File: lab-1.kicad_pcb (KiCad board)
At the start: 2 copper layers, 58.4 x 43.2 mm, 11 parts, among them U1 STM32F405RGTx

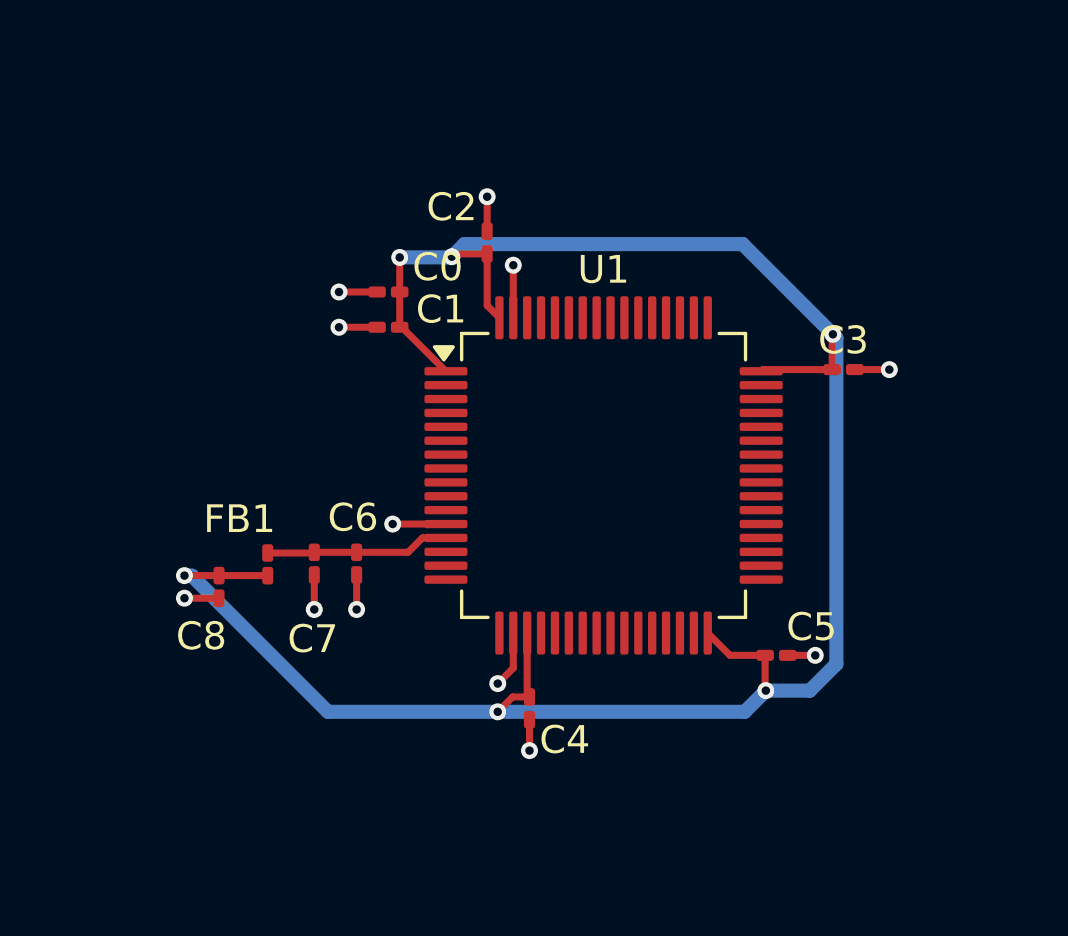
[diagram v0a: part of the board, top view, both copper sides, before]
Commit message: Changed the footprints + track width
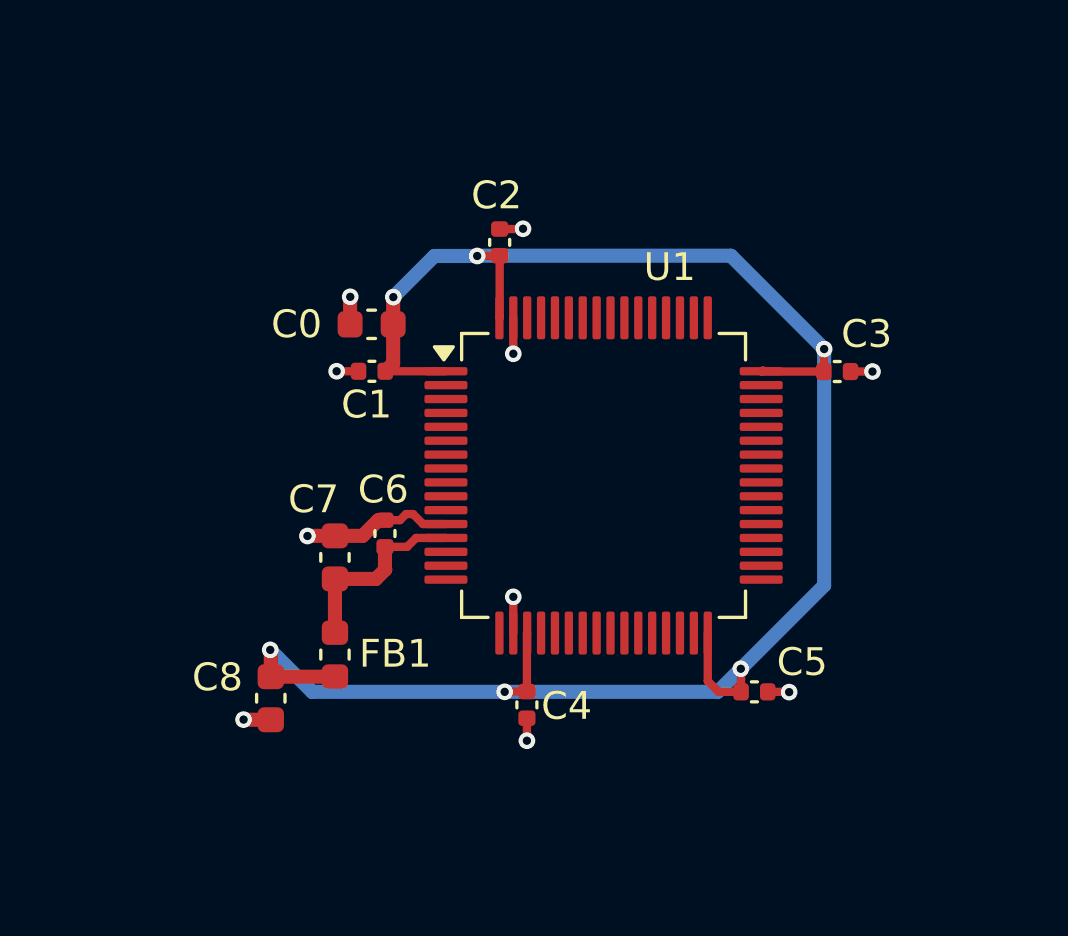
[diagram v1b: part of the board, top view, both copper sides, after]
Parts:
- C0, C7, C8: footprint Capacitor_SMD:C_0201_0603Metric_Pad0.64x0.40mm_HandSolder -> Capacitor_SMD:C_0603_1608Metric
- C1, C2, C3, C4, C5, C6: footprint Capacitor_SMD:C_0201_0603Metric_Pad0.64x0.40mm_HandSolder -> Capacitor_SMD:C_0402_1005Metric
- FB1: footprint Inductor_SMD:L_0201_0603Metric_Pad0.64x0.40mm_HandSolder -> Inductor_SMD:L_0603_1608Metric
- moved C8 4.42 mm to (145.5, 112.2)
- moved FB1 4.05 mm to (147.8, 110.6)
- moved C1 1.69 mm to (149.1, 100.4)
- moved C5 1.53 mm to (162.9, 111.9)
- moved C6 1.49 mm to (149.6, 106.2), turned to 90 degrees
- moved C0 1.31 mm to (149.1, 98.7)
- moved C7 0.78 mm to (147.8, 107.1), turned to 90 degrees
- moved C2 0.45 mm to (153.7, 95.8)
- moved C3 0.24 mm to (165.9, 100.4)
- moved C4 0.15 mm to (154.7, 112.4)
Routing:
- net +3.3V: track 78.2 -> 69.5 mm
- net GND: track 17.0 -> 14.0 mm, vias 12 -> 10

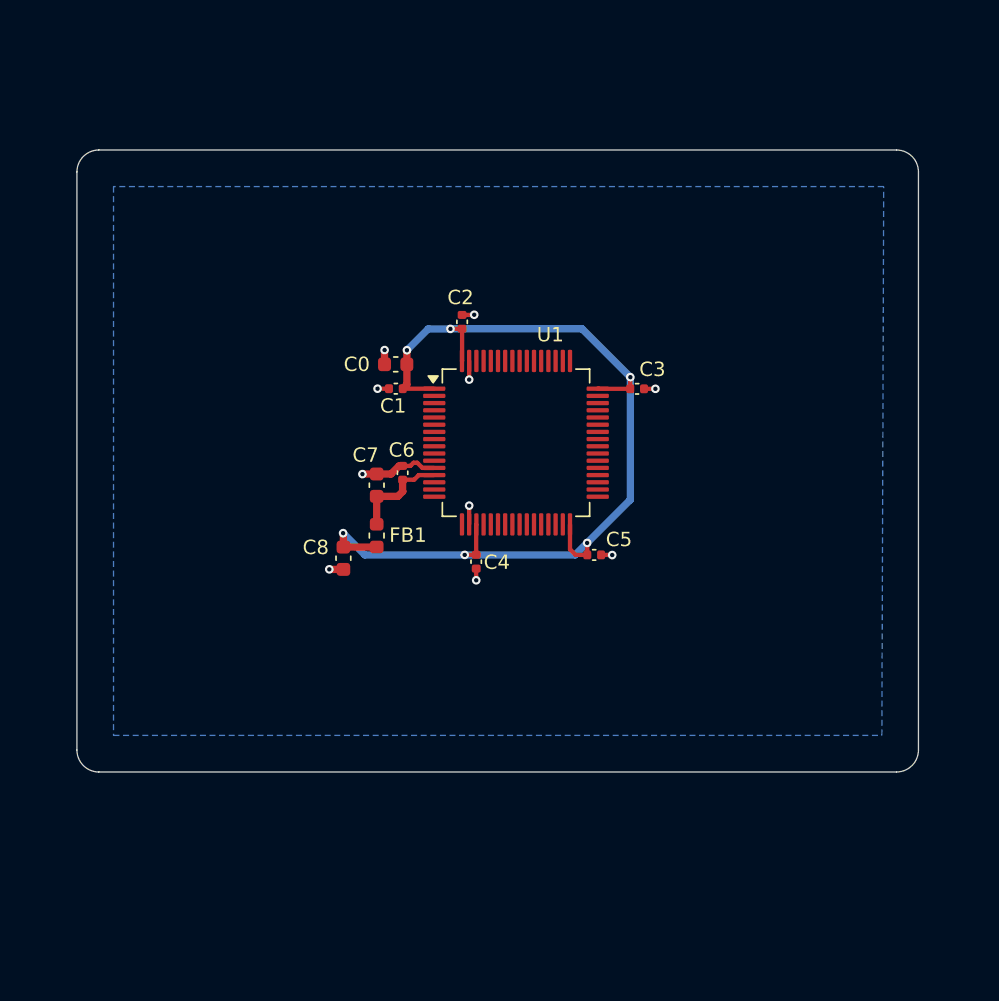
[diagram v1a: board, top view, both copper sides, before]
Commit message: Modified tracks and capacitor placing Added type-c and LDO MCP1700 as source of power for STM
Signed-off-by: Yehor Bilous <bilous801@gmail.com>
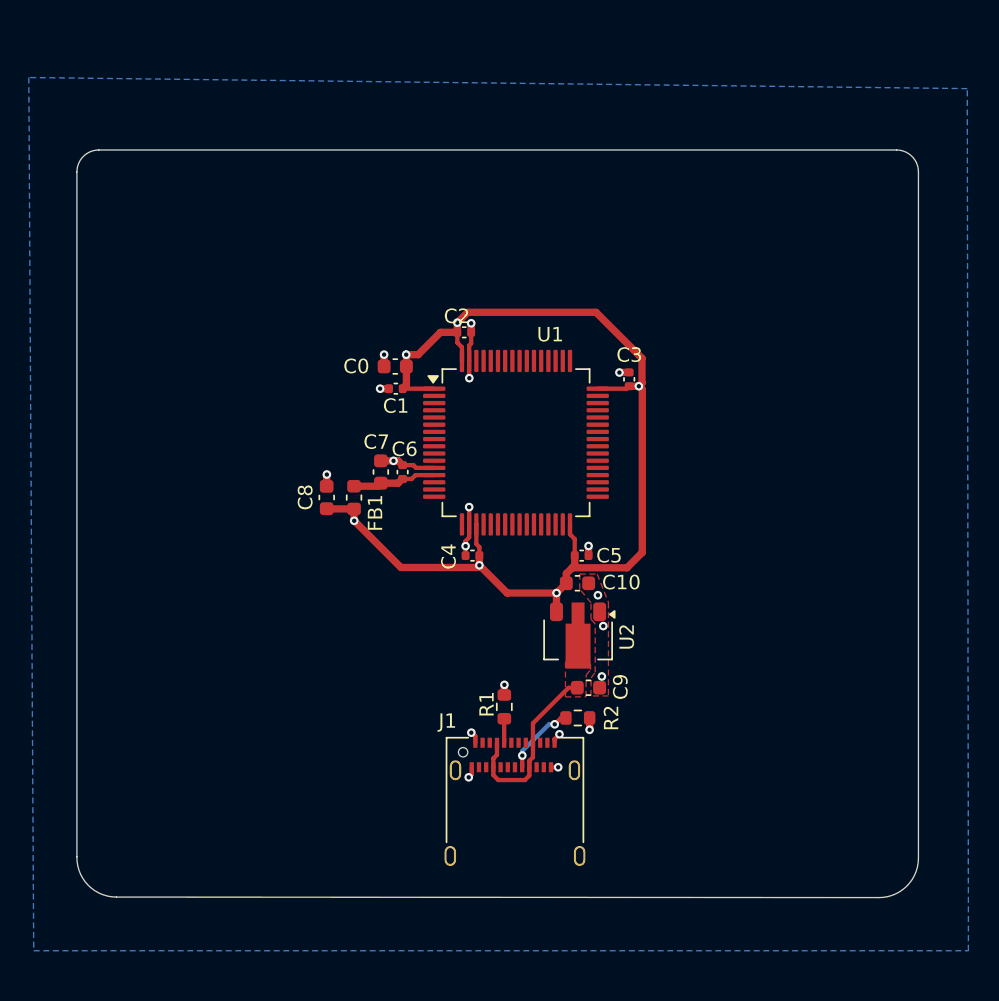
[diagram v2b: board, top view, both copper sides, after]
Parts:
- added C10: 1u, Capacitor_SMD:C_0603_1608Metric, F.Cu at (161.8, 113.9)
- added C9: 1u, Capacitor_SMD:C_0603_1608Metric, F.Cu at (162.5, 121.2)
- added J1: USB_C_Receptacle, Connector_USB:USB_C_Receptacle_Amphenol_12401610E4-2A, F.Cu at (157.4, 130.0)
- added R1: 5k1, Resistor_SMD:R_0603_1608Metric, F.Cu at (156.7, 122.5)
- added R2: 5k1, Resistor_SMD:R_0603_1608Metric, F.Cu at (161.8, 123.2)
- added U2: MCP1700x-120xxMB, Package_TO_SOT_SMD:SOT-89-3, F.Cu at (161.8, 117.8)
- C6: value 10n -> 100n
- FB1: value 120 -> ?
- moved C8 4.37 mm to (144.3, 107.9), turned to 90 degrees
- moved FB1 3.07 mm to (146.2, 108.0)
- moved C7 0.96 mm to (148.1, 106.2)
- moved C5 0.87 mm to (162.0, 112.0)
- moved C3 0.86 mm to (165.3, 99.7), turned to 90 degrees
- moved C2 0.75 mm to (153.9, 96.5), turned to 0 degrees
- moved C4 0.49 mm to (154.5, 112.0), turned to 180 degrees
- moved C0 0.15 mm to (149.1, 98.8)
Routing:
- net +5V: track 0.00 -> 13.0 mm
- net +3.3V: track 69.5 -> 76.7 mm
- net GND: track 14.0 -> 19.4 mm, vias 10 -> 19
- net Net-(J1-CC2): track 0.00 -> 5.10 mm, vias 0 -> 2
- net Net-(J1-CC1): track 0.00 -> 1.67 mm
- net +3.3VA: track 7.04 -> 5.88 mm
- added copper zone on F.Cu, net +5V
- added copper zone on F.Cu, net GND
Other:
- board size 58.4 x 43.2 mm -> 58.4 x 51.9 mm

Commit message: add a programmer header and power ORing
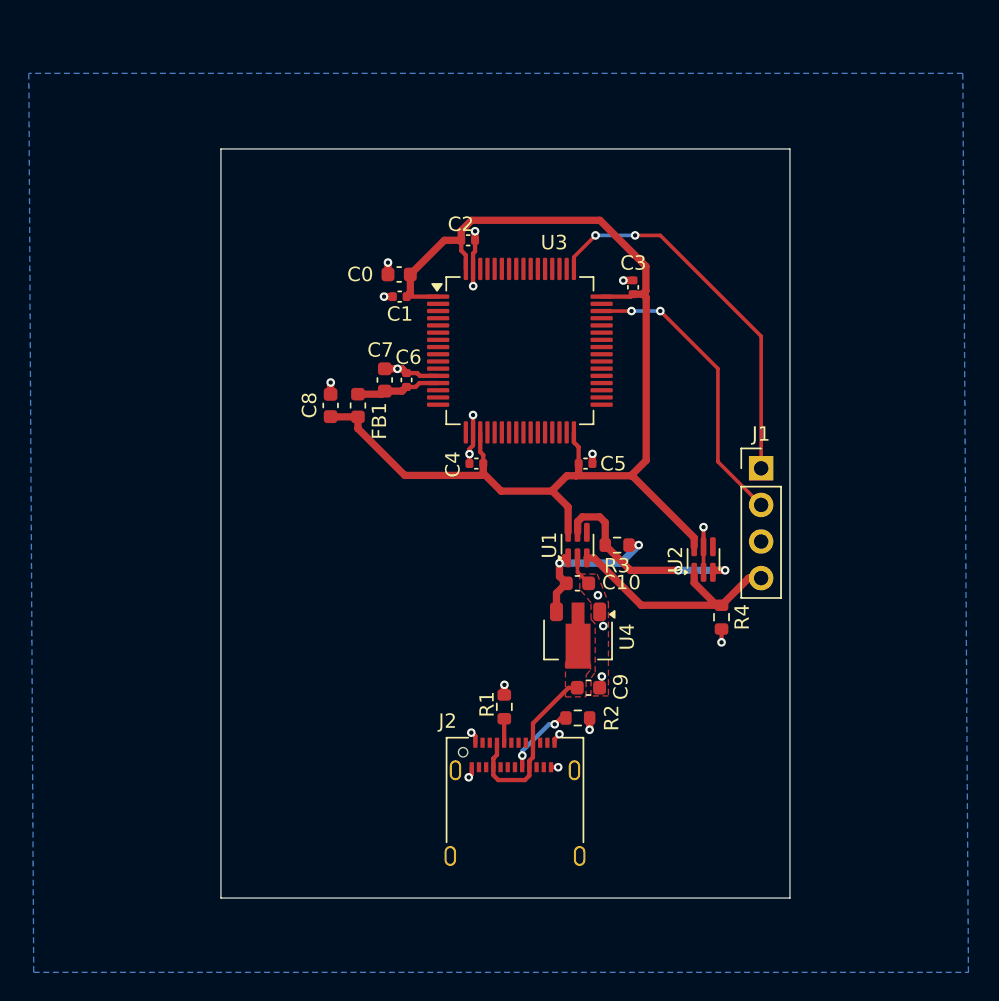
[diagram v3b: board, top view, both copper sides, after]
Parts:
- added J1: Conn_01x04_Pin, Connector_PinHeader_2.54mm:PinHeader_1x04_P2.54mm_Vertical, F.Cu at (174.5, 105.9)
- added R3: 10k, Resistor_SMD:R_0603_1608Metric, F.Cu at (164.5, 111.2)
- added R4: 100k, Resistor_SMD:R_0603_1608Metric, F.Cu at (171.8, 116.2)
- added U1: LM66100DCK, Package_TO_SOT_SMD:SOT-363_SC-70-6, F.Cu at (161.8, 111.2)
- added U2: LM66100DCK, Package_TO_SOT_SMD:SOT-363_SC-70-6, F.Cu at (170.5, 112.2)
- moved C0 6.40 mm to (149.4, 92.5)
- moved C1 6.40 mm to (149.4, 94.0)
- moved C2 6.40 mm to (154.2, 90.1)
- moved C3 6.40 mm to (165.6, 93.3)
- moved C4 6.40 mm to (154.7, 105.6)
- moved C5 6.40 mm to (162.3, 105.6)
- moved C6 6.40 mm to (149.9, 99.8)
- moved C7 6.40 mm to (148.4, 99.8)
- moved FB1 6.40 mm to (146.5, 101.6)
- moved U3 6.40 mm to (157.8, 97.8)
- moved C8 6.40 mm to (144.6, 101.6)
- renumbered J1 to J2, U1 to U3, U2 to U4
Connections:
- C10 pad 1: +3.3V -> +3.3V_LDO
- U3 pad 46: unconnected-(U1-PA13-Pad46) -> /SWDIO
- U3 pad 49: unconnected-(U1-PA14-Pad49) -> /SWCLK
- U4 pad 3: +3.3V -> +3.3V_LDO
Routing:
- net /SWCLK: track 0.00 -> 26.5 mm, vias 0 -> 2
- net /SWDIO: track 0.00 -> 20.4 mm, vias 0 -> 2
- net +3.3V_STLINK: track 0.00 -> 17.5 mm
- net Net-(U1-ST): track 0.00 -> 14.5 mm, vias 0 -> 2
- net +3.3V_LDO: track 0.00 -> 11.2 mm, vias 0 -> 2
- net +3.3V: track 76.7 -> 84.0 mm, vias 6 -> 0
- net GND: track 19.4 -> 25.6 mm, vias 19 -> 21
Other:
- board size 58.4 x 51.9 mm -> 39.5 x 52 mm

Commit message: add crystal
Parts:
- added C11: 22pF, Capacitor_SMD:C_0402_1005Metric, F.Cu at (146.0, 95.0)
- added C12: 22pF, Capacitor_SMD:C_0402_1005Metric, F.Cu at (146.0, 97.5)
- added Y1: 8 MHz, Crystal:Crystal_SMD_2520-4Pin_2.5x2.0mm, F.Cu at (148.9, 96.4)
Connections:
- U3 pad 5: unconnected-(U3-PH0-Pad5) -> /OSC_IN
- U3 pad 6: unconnected-(U3-PH1-Pad6) -> /OSC_OUT
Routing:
- net /OSC_OUT: track 0.00 -> 6.49 mm
- net /OSC_IN: track 0.00 -> 6.28 mm
- net GND: track 25.6 -> 27.4 mm, vias 21 -> 23

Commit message: Added buttons
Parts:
- added R5: 10k, Resistor_SMD:R_0402_1005Metric, F.Cu at (159.5, 87.5)
- added R6: 10k, Resistor_SMD:R_0402_1005Metric, F.Cu at (155.5, 87.5)
- added SW1: NRST, Button_Switch_THT:SW_PUSH_6mm_H4.3mm, F.Cu at (159.5, 79.0)
- added SW2: BOOT, Button_Switch_THT:SW_PUSH_6mm_H4.3mm, F.Cu at (148.8, 79.0)
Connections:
- U3 pad 60: unconnected-(U3-BOOT0-Pad60) -> /BOOT0
- U3 pad 7: unconnected-(U3-NRST-Pad7) -> /NRST
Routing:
- net /NRST: track 0.00 -> 29.7 mm, vias 0 -> 2
- net /BOOT0: track 0.00 -> 21.7 mm, vias 0 -> 2
- net +3.3V: track 84.0 -> 99.9 mm
- net GND: track 27.4 -> 28.4 mm, vias 23 -> 24
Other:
- board size 39.5 x 52 mm -> 39.5 x 59.5 mm

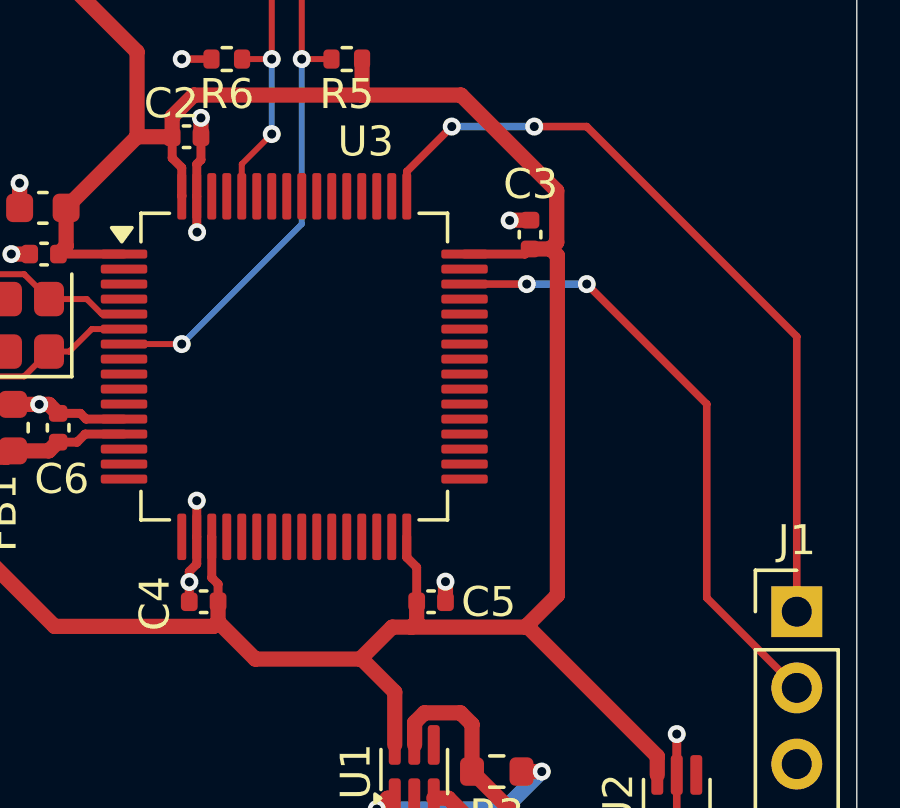
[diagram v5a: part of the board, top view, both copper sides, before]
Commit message: add VCAP
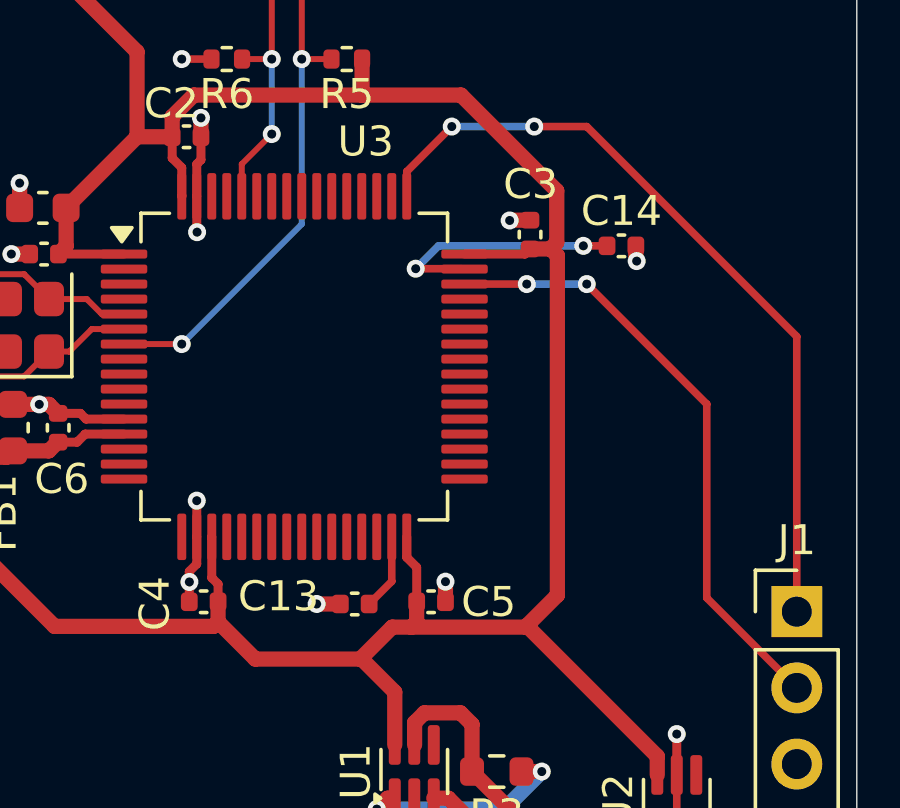
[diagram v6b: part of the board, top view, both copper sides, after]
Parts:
- added C13: 2.2u, Capacitor_SMD:C_0402_1005Metric, F.Cu at (159.8, 105.7)
- added C14: 2.2u, Capacitor_SMD:C_0402_1005Metric, F.Cu at (168.7, 93.7)
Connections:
- U3 pad 31: unconnected-(U3-VCAP_1-Pad31) -> Net-(U3-VCAP_1)
- U3 pad 47: unconnected-(U3-VCAP_2-Pad47) -> Net-(U3-VCAP_2)
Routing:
- net Net-(U3-VCAP_2): track 0.00 -> 8.33 mm, vias 0 -> 2
- net Net-(U3-VCAP_1): track 0.00 -> 2.55 mm
- net GND: track 28.4 -> 29.7 mm, vias 24 -> 26

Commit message: minor adjustments
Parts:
- removed R4: 100k, Resistor_SMD:R_0603_1608Metric
- moved R3 6.94 mm to (157.6, 112.0), turned to 0 degrees
- moved U2 6.64 mm to (164.0, 111.1)
- moved C14 5.19 mm to (163.8, 91.8)
- moved J1 4.46 mm to (170.3, 104.4)
- moved U1 1.35 mm to (160.4, 111.1)
- moved C12 0.87 mm to (146.9, 97.6)
- moved C11 0.84 mm to (146.8, 95.0)
- moved C1 0.64 mm to (149.7, 93.4)
- moved C6 0.62 mm to (150.5, 100.0)
- moved FB1 0.62 mm to (147.1, 101.7)
- moved C7 0.62 mm to (149.0, 100.0)
- moved C8 0.62 mm to (145.2, 101.7)
- moved Y1 0.59 mm to (149.5, 96.3)
- moved C5 0.46 mm to (162.8, 105.7)
- moved C3 0.40 mm to (165.3, 93.5)
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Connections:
- R3 pad 1: +3.3V_LDO -> GND
- R3 pad 2: Net-(U1-ST) -> +3.3V_LDO
- U1 pad 3: +3.3V_STLINK -> +3.3V
- U1 pad 5: Net-(U1-ST) -> GND
- U2 pad 3: Net-(U1-ST) -> +3.3V_LDO
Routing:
- net Net-(U1-ST): track 14.5 -> 0.00 mm, vias 2 -> 0
- net +3.3V_STLINK: track 17.5 -> 8.61 mm
- net GND: track 29.7 -> 38.0 mm, vias 26 -> 22
- net Net-(U3-VCAP_2): track 8.33 -> 4.44 mm, vias 2 -> 0
- net +3.3V_LDO: track 11.2 -> 15.0 mm
- net /SWCLK: track 26.5 -> 22.9 mm
- net /SWDIO: track 20.4 -> 17.3 mm
- net /OSC_OUT: track 6.49 -> 5.55 mm
- net /OSC_IN: track 6.28 -> 5.58 mm
- net /NRST: track 29.7 -> 30.2 mm
- net +3.3V: track 99.9 -> 100.4 mm
- net +3.3VA: track 5.88 -> 5.37 mm
- removed copper zone on F.Cu, net GND
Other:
- board size 39.5 x 59.5 mm -> 29.7 x 59.5 mm
